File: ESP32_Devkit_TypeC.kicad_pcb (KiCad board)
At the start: 2 copper layers, 25.3 x 48.2 mm, 57 parts, among them J1 USB_C_Receptacle_USB2.0, J2 Conn_01x19, J3 Conn_01x19, Q1 SS8050, Q2 SS8050, SW1 EN, SW2 BOOT, U1 MP2359, U2 CH340G, U3 ESP32-PICO-D4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

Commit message: Migrated project to Kicad 6.0, removed unnecessary files
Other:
- net class Default removed

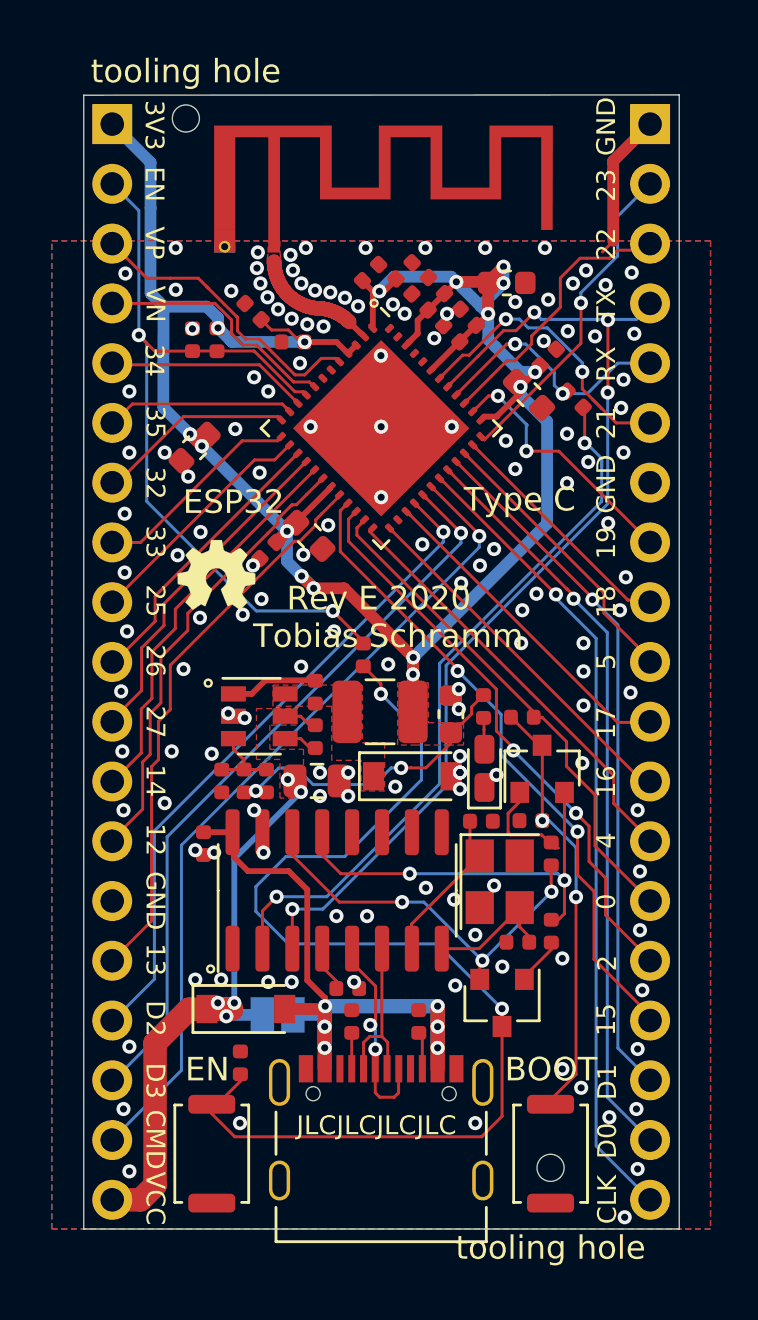
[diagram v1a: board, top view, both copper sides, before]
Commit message: Updated footprints, reconnected CH340C
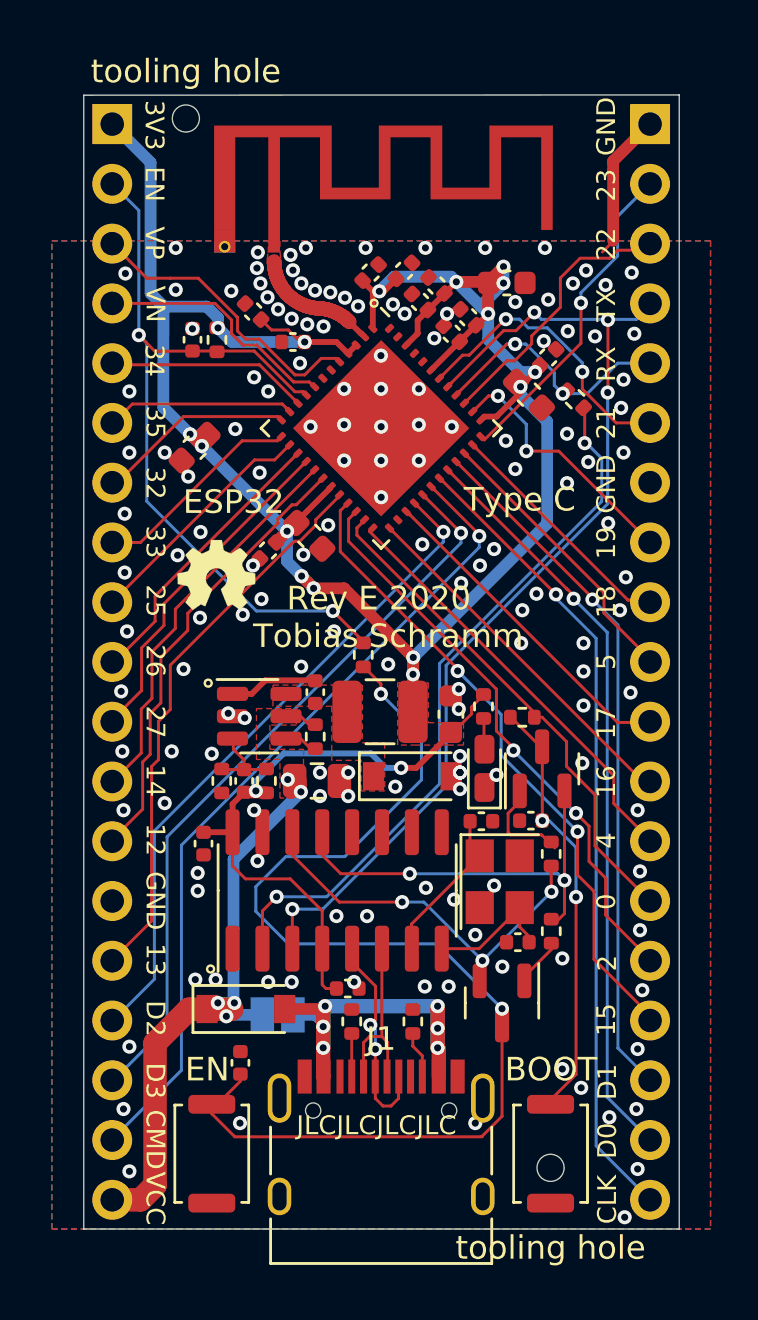
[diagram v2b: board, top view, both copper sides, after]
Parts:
- J1: footprint Connector_USB:USB_C_Receptacle_Palconn_UTC16-G -> Moucha_Connectors:USBC_Receptacle_TYPE-C-31-M-12
- R5: value 49.9kR -> 56kR
- R6: value 15 kR -> 18 kR
- U1: value MP2359 -> MP2259
- U2: value CH340G -> CH340C
- moved J1 1.87 mm to (100.0, 121.7)
- moved R3 0.25 mm to (101.3, 115.3)
- turned C5 to 180 degrees
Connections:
- C5 pad 1: Net-(C5-Pad1) -> GND
- C5 pad 2: GND -> +3V3
- C7 pad 2: VBUS -> +3V3
- J1 pad A8: Net-(J1-PadA8) -> unconnected-(J1-PadA8)
- J1 pad B8: Net-(J1-PadB8) -> unconnected-(J1-PadB8)
- U2 pad 10: Net-(U2-Pad10) -> unconnected-(U2-Pad10)
- U2 pad 11: Net-(U2-Pad11) -> unconnected-(U2-Pad11)
- U2 pad 12: Net-(U2-Pad12) -> unconnected-(U2-Pad12)
- U2 pad 16: VBUS -> +3V3
- U2 pad 4: Net-(C5-Pad1) -> +3V3
- U2 pad 9: Net-(U2-Pad9) -> unconnected-(U2-Pad9)
- U3 pad 26: Net-(U3-Pad26) -> unconnected-(U3-Pad26)
- U3 pad 44: Net-(U3-Pad44) -> unconnected-(U3-Pad44)
- U3 pad 45: Net-(U3-Pad45) -> unconnected-(U3-Pad45)
- U3 pad 47: Net-(U3-Pad47) -> unconnected-(U3-Pad47)
- U3 pad 48: Net-(U3-Pad48) -> unconnected-(U3-Pad48)
- U3 pad 6: Net-(U3-Pad6) -> unconnected-(U3-Pad6)
- U3 pad 7: Net-(U3-Pad7) -> unconnected-(U3-Pad7)
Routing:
- net +3V3: track 109.5 -> 121.6 mm
- net VBUS: track 28.2 -> 17.5 mm
- net Net-(C5-Pad1): track 1.94 -> 0.00 mm
- net /IO21: track 13.2 -> 12.5 mm
- net Net-(J1-PadA6): track 8.86 -> 9.44 mm
- net GND: track 6.70 -> 6.68 mm, vias 145 -> 154

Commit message: Changed button type, DRC fixes
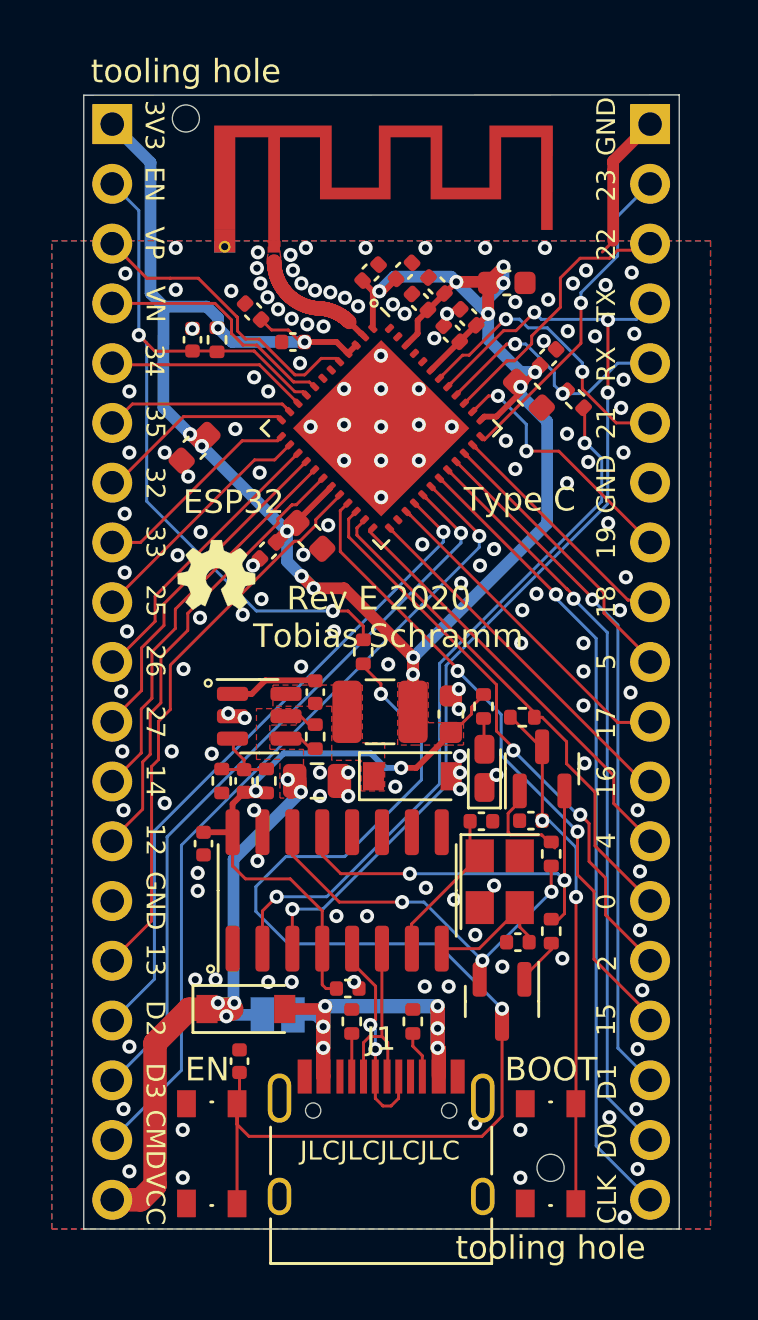
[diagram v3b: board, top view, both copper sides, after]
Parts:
- SW1, SW2: footprint Button_Switch_SMD:SW_Push_SPST_NO_Alps_SKRK -> Moucha_Primitives:SW_Push_1P1T_Vertical_3x4mm
- moved R11 0.13 mm to (99.2, 99.6)
- moved C10 0.08 mm to (94.0, 117.0)
- moved Q1 0.06 mm to (105.1, 114.4)
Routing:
- net Net-(C11-Pad2): track 18.4 -> 22.0 mm
- net Net-(C10-Pad2): track 48.0 -> 50.9 mm

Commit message: updated documentation
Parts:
- J1: footprint Moucha_Connectors:USBC_Receptacle_TYPE-C-31-M-12 -> Connector_USB:USB_C_Receptacle_HRO_TYPE-C-31-M-12
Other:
- board text added: "Rev F 2022"
- board text removed: "Rev E 2020"

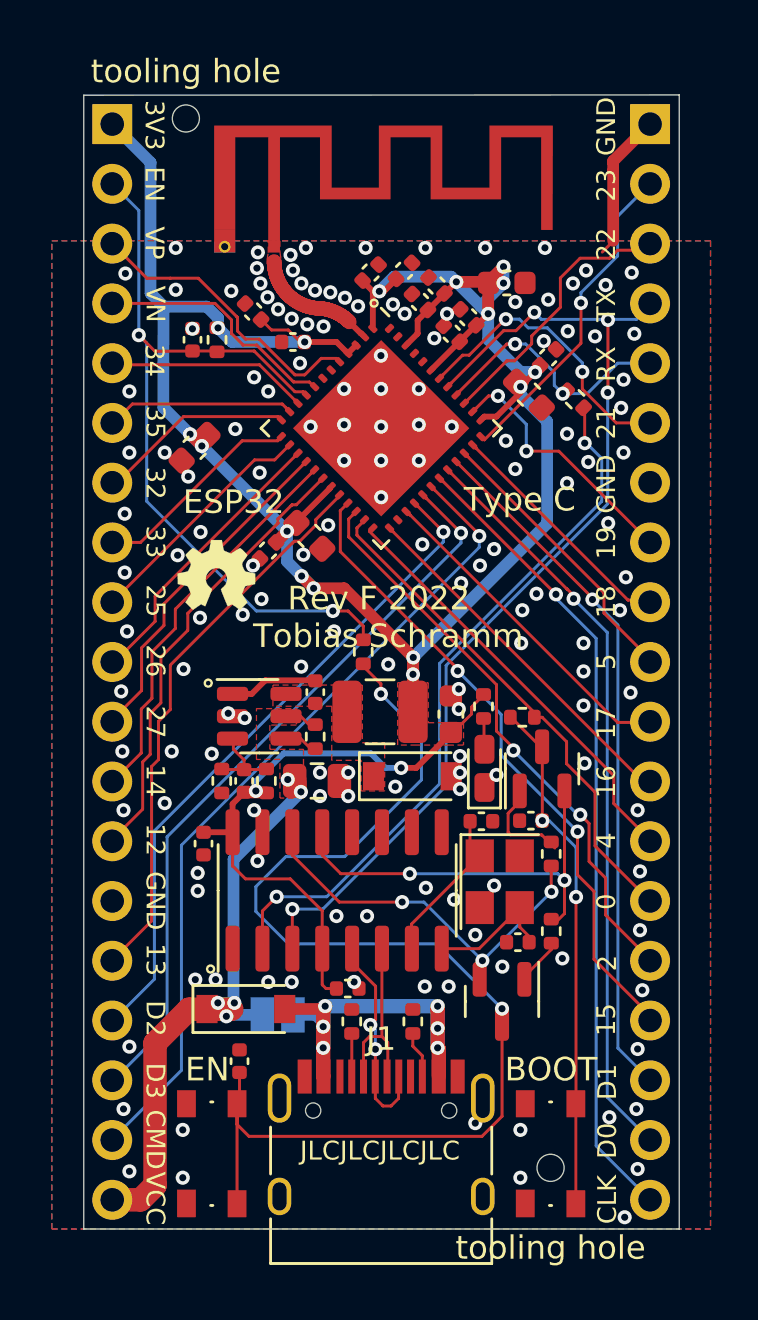
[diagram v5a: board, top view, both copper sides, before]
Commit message: Rev EB serial transciever bugfix, component upgrade
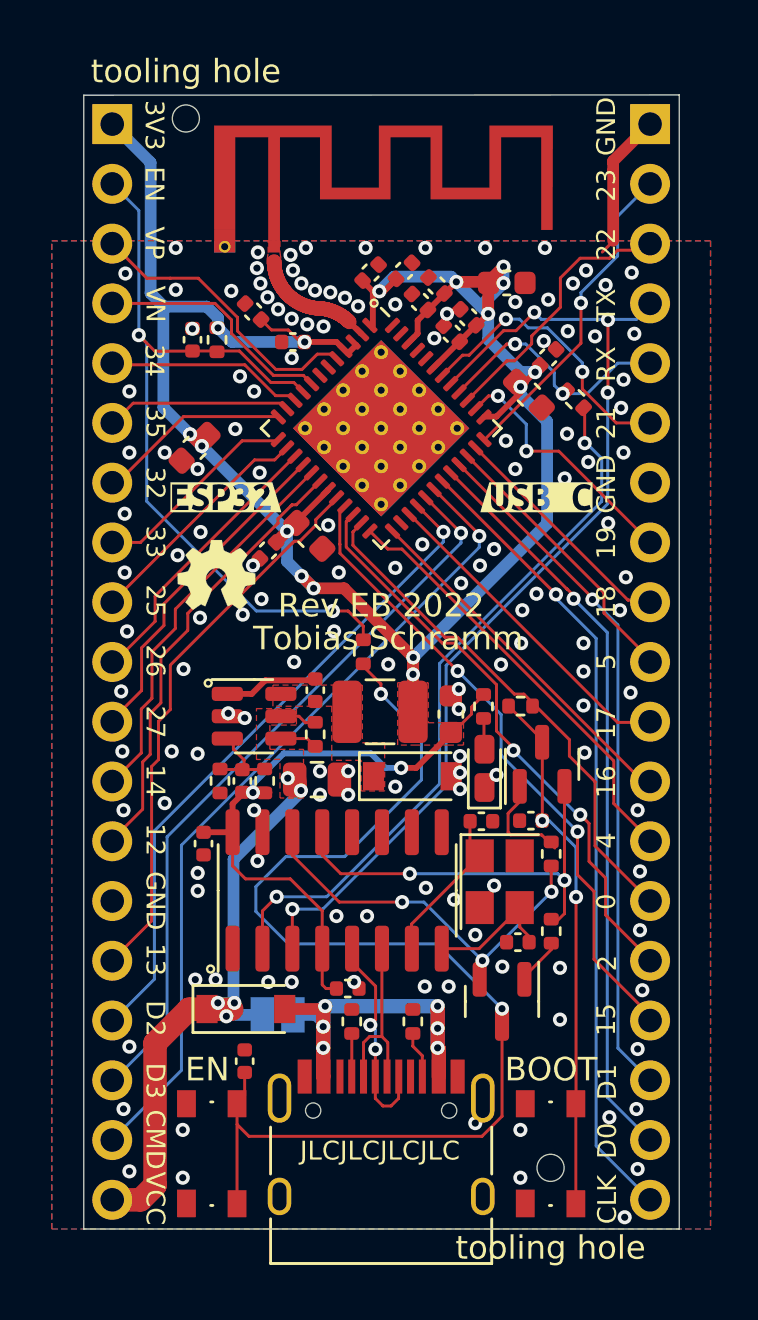
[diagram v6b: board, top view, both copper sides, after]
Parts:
- added kibuzzard-62337F52: G***, kibuzzard-62337F52, F.Cu at (106.6, 93.0)
- added kibuzzard-62337F79: G***, kibuzzard-62337F79, F.Cu at (93.4, 93.0)
- U3: footprint Package_ESP32:ESP32-Pico-D4 -> Package_ESP32:ESP32-Pico-D4-Handsolder
- moved R12 0.48 mm to (105.9, 101.9)
- moved C10 0.22 mm to (94.2, 117.0)
- moved U1 0.22 mm to (94.6, 102.3)
- moved Q2 0.19 mm to (106.8, 104.3)
- moved R1 0.10 mm to (97.2, 103.1)
- moved C1 0.08 mm to (97.2, 101.2)
- moved C9 0.08 mm to (94.1, 105.1)
- moved R5 0.08 mm to (95.0, 105.1)
- moved R6 0.07 mm to (93.2, 105.1)
- moved C3 0.06 mm to (97.3, 105.0)
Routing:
- net Net-(C10-Pad2): track 50.9 -> 48.9 mm
- net /IO16: track 15.7 -> 14.8 mm
- net +3V3: track 121.6 -> 120.8 mm
- net Net-(J1-PadA6): track 9.44 -> 8.85 mm
- net Net-(C2-Pad1): track 7.31 -> 6.72 mm
- net Net-(C11-Pad2): track 22.0 -> 22.6 mm
- net GND: vias 154 -> 143
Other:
- board text added: "Rev EB 2022"
- board text removed: "ESP32"
- board text removed: "Rev F 2022"
- board text removed: "Type C"

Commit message: Rev EC
updated ESP32 footprint based on datasheet, minor silkscreen fixes
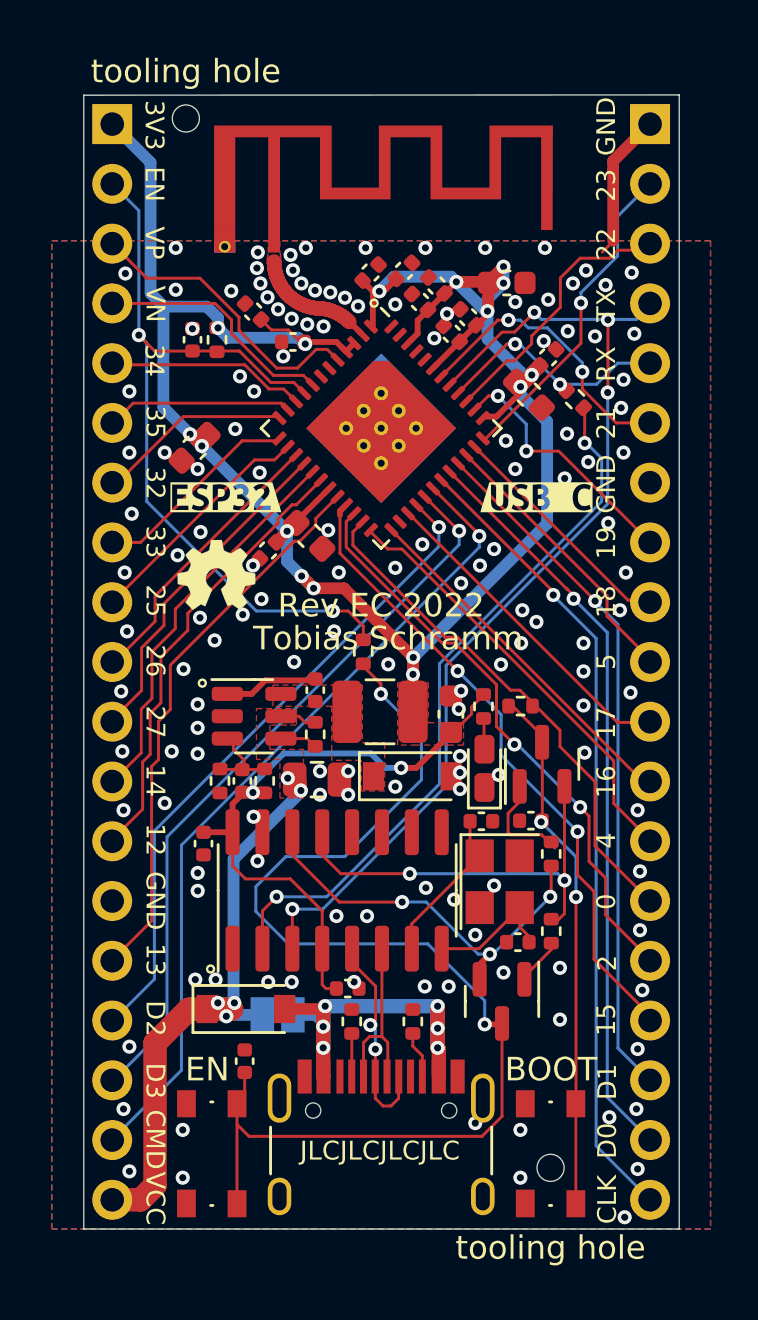
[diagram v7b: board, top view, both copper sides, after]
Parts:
- U3: footprint Package_ESP32:ESP32-Pico-D4-Handsolder -> Package_ESP32:ESP32-Pico-D4-Thermal
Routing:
- net Net-(C11-Pad2): track 22.6 -> 21.7 mm
- net Net-(C10-Pad2): track 48.9 -> 49.8 mm
- net /RXD: track 10.7 -> 10.1 mm
- net GND: vias 143 -> 144
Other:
- rule pad_to_mask_clearance: 0.01 -> 0
- board text added: "Rev EC 2022"
- board text removed: "Rev EB 2022"
